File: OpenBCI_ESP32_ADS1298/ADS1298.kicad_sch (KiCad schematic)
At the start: 30 parts, among them J2 Conn_02x08_Odd_Even, J3 Conn_02x03_Odd_Even, J4 Conn_02x02_Odd_Even, U7 ADS1299IPAG1

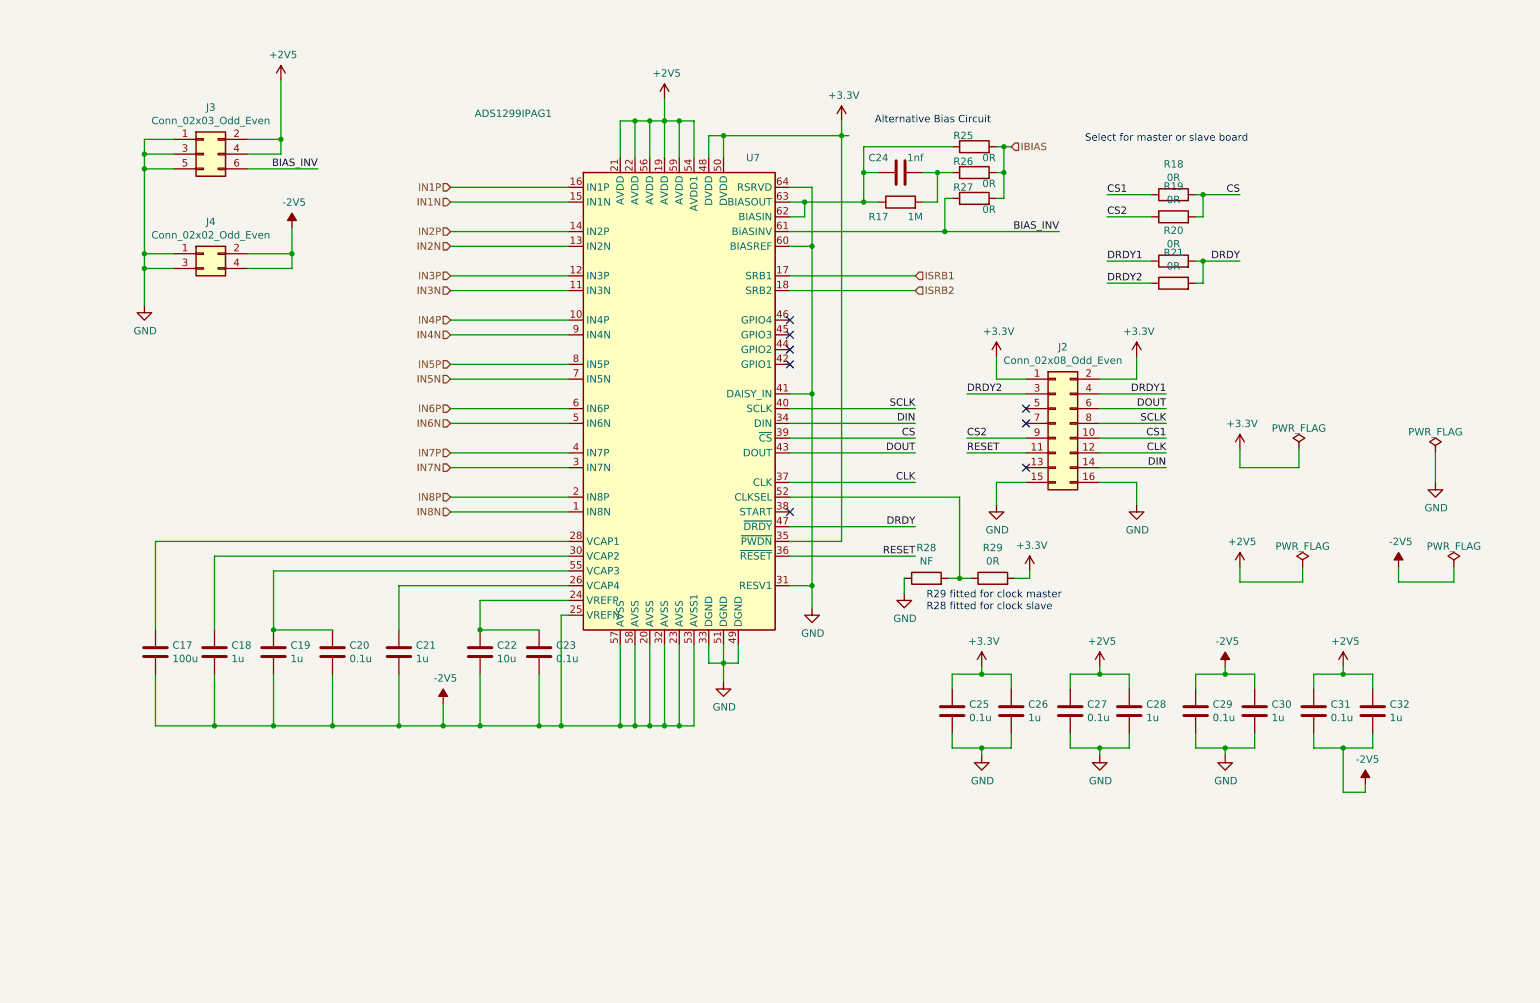
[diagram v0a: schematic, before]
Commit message: add ADS1298 files
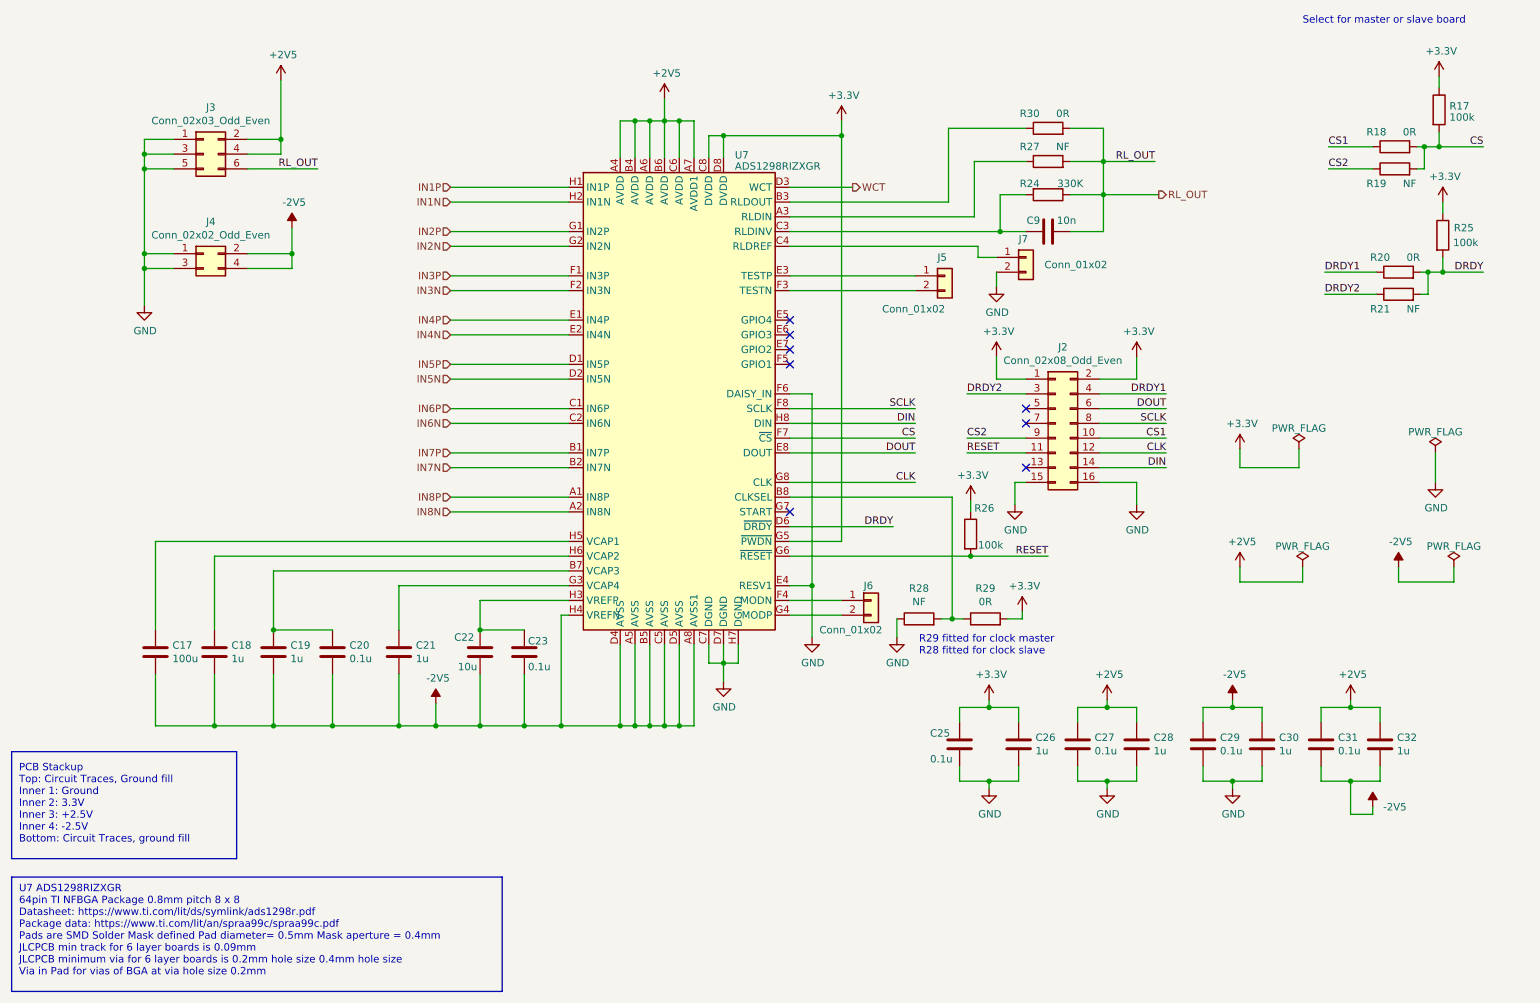
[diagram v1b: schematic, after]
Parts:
- removed C24: 1nf, Capacitor_SMD:C_0603_1608Metric, symbol Device:C
- removed U7: ADS1299IPAG1, Package_QFP:TQFP-64_10x10mm_P0.5mm, symbol OpenBCI_ESP32:ADS1299IPAG1
- added C9: 10n, Capacitor_SMD:C_0603_1608Metric, symbol Device:C
- added J5, J6, J7: Conn_01x02, Connector_PinHeader_2.00mm:PinHeader_1x02_P2.00mm_Vertical, symbol Connector_Generic:Conn_01x02
- added R24: 330K, Resistor_SMD:R_0603_1608Metric, symbol Device:R
- added R30: 0R, Resistor_SMD:R_0603_1608Metric, symbol Device:R
- added U7: ADS1298RIZXGR, OpenBCI_ESP32:BGA-64_8x8_8.0x8.0mm, symbol OpenBCI_ESP32:ADS1298RIZXGR
- R17: value 1M -> 100k
- R19, R21, R27: value 0R -> NF
- R25, R26: value 0R -> 100k
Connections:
- net +2V5: now also U7.A4 (AVDD), U7.A6 (AVDD), U7.A7 (AVDD1), U7.B4 (AVDD), U7.B6 (AVDD), U7.C6 (AVDD)
- net +3.3V: now also R17.1, R25.1, R26.1, U7.C8 (DVDD), U7.D8 (DVDD), U7.G5 (~{PWDN})
- net -2V5: now also U7.A5 (AVSS), U7.A8 (AVSS1), U7.B5 (AVSS), U7.C5 (AVSS), U7.D4 (AVSS), U7.D5 (AVSS), U7.H4 (VREFN)
- net CLK: now also U7.G8 (CLK)
- net CS: now also R17.2, U7.F7 (~{CS})
- net DIN: now also U7.H8 (DIN)
- net DOUT: now also U7.E8 (DOUT)
- net DRDY: now also R25.2, U7.D6 (~{DRDY})
- net GND: now also J7.2 (Pin_2), U7.C7 (DGND), U7.D7 (DGND), U7.E4 (RESV1), U7.F6 (DAISY_IN), U7.H7 (DGND)
- net IN1N: now also U7.H2 (IN1N)
- net IN1P: now also U7.H1 (IN1P)
- net IN2N: now also U7.G2 (IN2N)
- net IN2P: now also U7.G1 (IN2P)
- net IN3N: now also U7.F2 (IN3N)
- net IN3P: now also U7.F1 (IN3P)
- net IN4N: now also U7.E2 (IN4N)
- net IN4P: now also U7.E1 (IN4P)
- net IN5N: now also U7.D2 (IN5N)
- net IN5P: now also U7.D1 (IN5P)
- net IN6N: now also U7.C2 (IN6N)
- net IN6P: now also U7.C1 (IN6P)
- net IN7N: now also U7.B2 (IN7N)
- net IN7P: now also U7.B1 (IN7P)
- net IN8N: now also U7.A2 (IN8N)
- net IN8P: now also U7.A1 (IN8P)
- net RESET: now also R26.2, U7.G6 (~{RESET})
- net SCLK: now also U7.F8 (SCLK)
- net at C22.1, C23.1: now also U7.H3 (VREFP)
- net at C21.1: now also U7.G3 (VCAP4)
- net at C17.1: now also U7.H5 (VCAP1)
- net at C18.1: now also U7.H6 (VCAP2)
- net at R28.2, R29.1: now also U7.B8 (CLKSEL)
- net at C19.1, C20.1: now also U7.B7 (VCAP3)
- net BIAS_INV: no longer names the net of R27.1
- net BIAS_INV: now also U7.A3 (RLDIN); no longer J3.6 (Pin_6)
- removed net IBIAS: R25.2, R26.2, R27.2
- new net: J7.1 (Pin_1), U7.C4 (RLDREF)
- new net: C9.1, R24.2, U7.C3 (RLDINV)
- new net: J6.1 (Pin_1), U7.F4 (MODN)
- new net: J6.2 (Pin_2), U7.G4 (MODP)
- new net: J5.1 (Pin_1), U7.E3 (TESTP)
- new net: J5.2 (Pin_2), U7.F3 (TESTN)
- new net: R30.1, U7.B3 (RLDOUT)
- new net RL_OUT: C9.2, J3.6 (Pin_6), R24.1, R27.2, R30.2
- new net WCT: U7.D3 (WCT)
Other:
- note added: "PCB Stackup Top: Circuit Traces, Ground fill Inner 1: Ground Inner 2: 3.3V Inner 3: +2.5V Inner 4: -2.5V Bottom: Circuit Traces, ground fill"
- note added: "U7 ADS1298RIZXGR 64pin TI NFBGA Package 0.8mm pitch 8 x 8 Datasheet: https://www.ti.com/lit/ds/symlink/ads1298r.pdf Package data: https://www.ti.com/lit/an/spraa99c/spraa99c.pdf Pads are SMD Solder Mask defined Pad diameter= 0.5mm Mask aperture = 0.4mm JLCPCB min track for 6 layer boards is 0.09mm JLCPCB minimum via for 6 layer boards is 0.2mm hole size 0.4mm hole size Via in Pad for vias of BGA 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"
- note removed: "Alternative Bias Circuit"
- moved on the sheet: C23, C25, C26, C27, C28, C29, C30, C31, C32, R18, R19, R20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
